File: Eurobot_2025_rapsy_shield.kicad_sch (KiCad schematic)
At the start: 30 parts, among them J1 Raspberry_Pi_2_3, J2 SPI, J4 Conn_01x02, J5 AU, J6 Conn_01x04, Q1 2N7002, Q2 2N7002, U1 TPS54302

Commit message: v1 ok
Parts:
- added C_Act1, C_Act2: Conn_02x05_Odd_Even, Connector_IDC:IDC-Header_2x05_P2.54mm_Vertical, symbol Connector_Generic:Conn_02x05_Odd_Even
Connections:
- net GND: now also C_Act1.6 (Pin_6), C_Act2.6 (Pin_6)
- net C_Act1-3: now reaches J1.11 (GPIO17)
- net C_Act1-3: now also C_Act1.7 (Pin_7)
- net C_Act1-9: now reaches J1.12 (GPIO18/PWM0)
- net C_Act1-9: now also C_Act1.5 (Pin_5)
- net C_Act1-2: now reaches J1.13 (GPIO27)
- net C_Act1-2: now also C_Act1.3 (Pin_3)
- net C_Act1-4: now reaches J1.15 (GPIO22)
- net C_Act1-4: now also C_Act1.4 (Pin_4)
- net C_Act1-6: now reaches J1.16 (GPIO23)
- net C_Act1-6: now also C_Act1.1 (Pin_1)
- net C_Act1-8: now reaches J1.22 (GPIO25)
- net C_Act1-8: now also C_Act1.2 (Pin_2)
- net C_Act2-8: now reaches J1.29 (GCLK1/GPIO5)
- net C_Act2-8: now also C_Act2.9 (Pin_9)
- net C_Act1-1: now reaches J1.3 (SDA/GPIO2)
- net C_Act1-1: now also C_Act1.10 (Pin_10)
- net C_Act2-4: now reaches J1.31 (GCLK2/GPIO6)
- net C_Act2-4: now also C_Act2.10 (Pin_10)
- net C_Act2-2: now reaches J1.32 (PWM0/GPIO12)
- net C_Act2-2: now also C_Act2.7 (Pin_7)
- net C_Act2-6: now reaches J1.33 (PWM1/GPIO13)
- net C_Act2-6: now also C_Act2.8 (Pin_8)
- net C_Act2-7: now reaches J1.35 (GPIO19/MISO1)
- net C_Act2-7: now also C_Act2.4 (Pin_4)
- net C_Act2-1: now reaches J1.36 (GPIO16)
- net C_Act2-1: now also C_Act2.5 (Pin_5)
- net C_Act2-5: now reaches J1.37 (GPIO26)
- net C_Act2-5: now also C_Act2.1 (Pin_1)
- net C_Act2-9: now reaches J1.38 (GPIO20/MOSI1)
- net C_Act2-9: now also C_Act2.3 (Pin_3)
- net C_Act2-3: now reaches J1.40 (GPIO21/SCLK1)
- net C_Act2-3: now also C_Act2.2 (Pin_2)
- net C_Act1-5: now reaches J1.5 (SCL/GPIO3)
- net C_Act1-5: now also C_Act1.9 (Pin_9)
- net C_Act1-7: now reaches J1.7 (GCLK0/GPIO4)
- net C_Act1-7: now also C_Act1.8 (Pin_8)

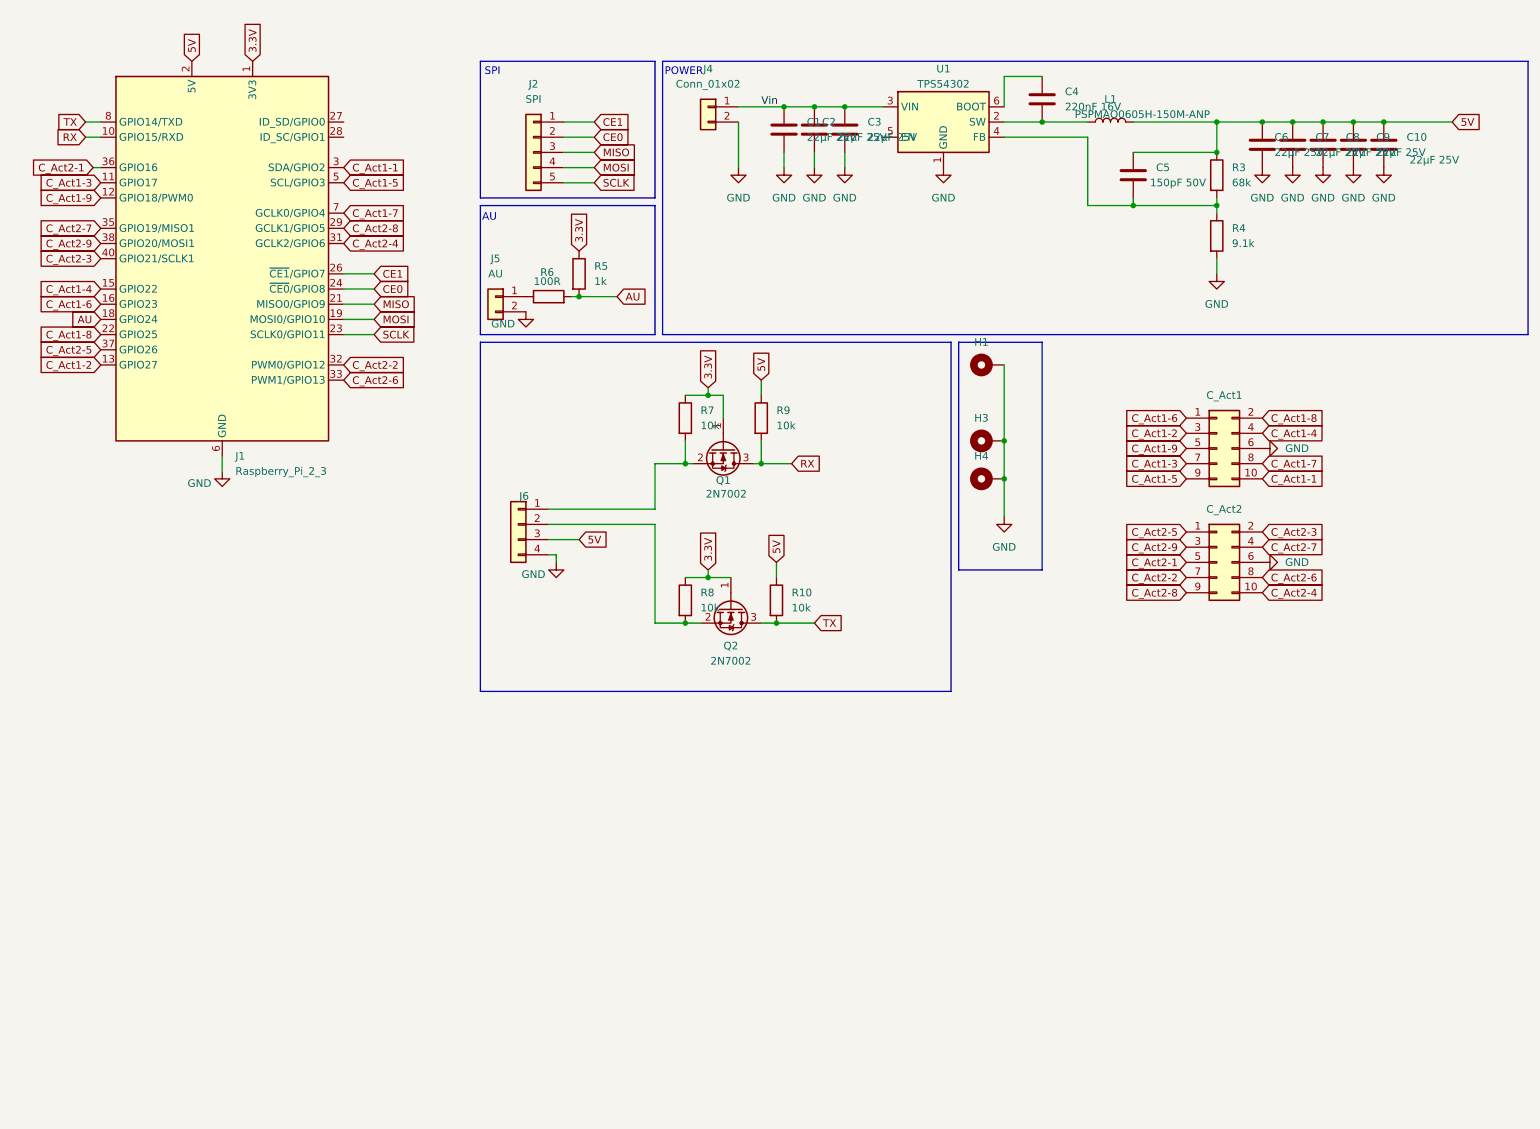
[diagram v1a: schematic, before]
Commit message: schematic for can
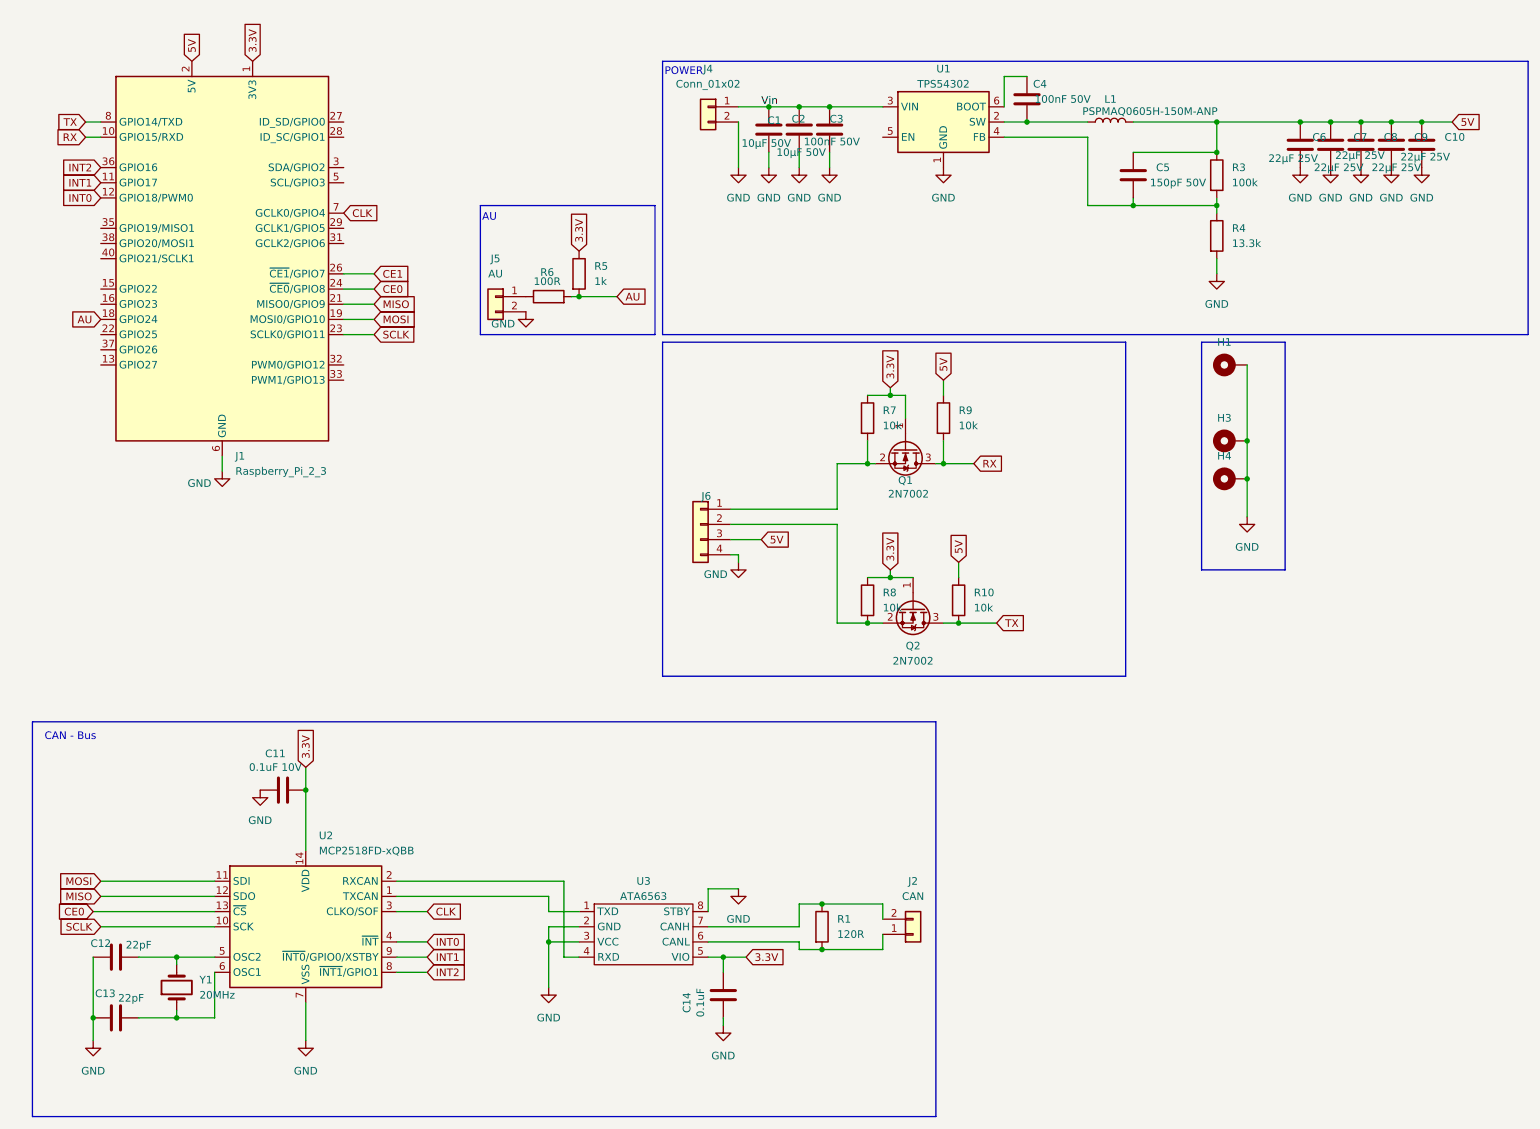
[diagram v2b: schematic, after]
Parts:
- removed C_Act1, C_Act2: Conn_02x05_Odd_Even, Connector_IDC:IDC-Header_2x05_P2.54mm_Vertical, symbol Connector_Generic:Conn_02x05_Odd_Even
- removed J2: SPI, Connector_JST:JST_XH_B5B-XH-A_1x05_P2.50mm_Vertical, symbol Connector_Generic:Conn_01x05
- added C11: 0.1uF 10V, Capacitor_SMD:C_0805_2012Metric, symbol Device:C
- added C12, C13: 22pF, Capacitor_SMD:C_0805_2012Metric, symbol Device:C
- added C14: 0.1uF, Capacitor_SMD:C_0805_2012Metric, symbol Device:C
- added J2: CAN, Connector_JST:JST_XH_B2B-XH-A_1x02_P2.50mm_Vertical, symbol Connector_Generic:Conn_01x02
- added R1: 120R, Resistor_SMD:R_0603_1608Metric, symbol Device:R
- added U2: MCP2518FD-xQBB, symbol Interface_CAN_LIN:MCP2518FD-xQBB
- added U3: ATA6563, Package_SO:SOIC-8_3.9x4.9mm_P1.27mm, symbol Custom:ATA6563-GAQW1
- added Y1: 20MHz, Crystal:Crystal_SMD_0603-2Pin_6.0x3.5mm, symbol Device:Crystal
- C1, C2: value 22µF 25V -> 10µF 50V
- C3: value 22µF 25V -> 100nF 50V
- C4: value 220nF 16V -> 100nF 50V
- R3: value 68k -> 100k
- R4: value 9.1k -> 13.3k
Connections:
- net 3.3V: now also C11.2, C14.2, U2.14 (VDD), U3.5 (VIO)
- net CE0: now also U2.13 (~{CS})
- net GND: now also C11.1, C12.1, C13.1, C14.1, U2.15 (VSS), U2.7 (VSS), U3.2 (GND), U3.3 (VCC), U3.8 (STBY)
- net MISO: now also U2.12 (SDO)
- net MOSI: now also U2.11 (SDI)
- net SCLK: now also U2.10 (SCK)
- net C_Act1-1: no longer names the net of J1.3 (SDA/GPIO2)
- net C_Act1-2: no longer names the net of J1.13 (GPIO27)
- net C_Act1-3 renamed INT1
- net INT1: now also U2.9 (~{INT0}/GPIO0/XSTBY)
- net C_Act1-4: no longer names the net of J1.15 (GPIO22)
- net C_Act1-5: no longer names the net of J1.5 (SCL/GPIO3)
- net C_Act1-6: no longer names the net of J1.16 (GPIO23)
- net C_Act1-7 renamed CLK
- net CLK: now also U2.3 (CLKO/SOF)
- net C_Act1-8: no longer names the net of J1.22 (GPIO25)
- net C_Act1-9 renamed INT0
- net INT0: now also U2.4 (~{INT})
- net C_Act2-1 renamed INT2
- net INT2: now also U2.8 (~{INT1}/GPIO1)
- net C_Act2-2: no longer names the net of J1.32 (PWM0/GPIO12)
- net C_Act2-3: no longer names the net of J1.40 (GPIO21/SCLK1)
- net C_Act2-4: no longer names the net of J1.31 (GCLK2/GPIO6)
- net C_Act2-5: no longer names the net of J1.37 (GPIO26)
- net C_Act2-6: no longer names the net of J1.33 (PWM1/GPIO13)
- net C_Act2-7: no longer names the net of J1.35 (GPIO19/MISO1)
- net C_Act2-8: no longer names the net of J1.29 (GCLK1/GPIO5)
- net C_Act2-9: no longer names the net of J1.38 (GPIO20/MOSI1)
- new net: C12.2, U2.5 (OSC2), Y1.2
- new net: C13.2, U2.6 (OSC1), Y1.1
- new net: U2.1 (TXCAN), U3.1 (TXD)
- new net: U2.2 (RXCAN), U3.4 (RXD)
- new net: J2.1 (Pin_1), R1.2, U3.6 (CANL)
- new net: J2.2 (Pin_2), R1.1, U3.7 (CANH)
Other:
- note added: "CAN - Bus"
- note removed: "SPI"
- moved on the sheet: C1, C10, C2, C3, C4, C6, C7, C8, C9, H1, H3, H4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
